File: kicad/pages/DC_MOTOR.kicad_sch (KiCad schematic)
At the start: 15 parts

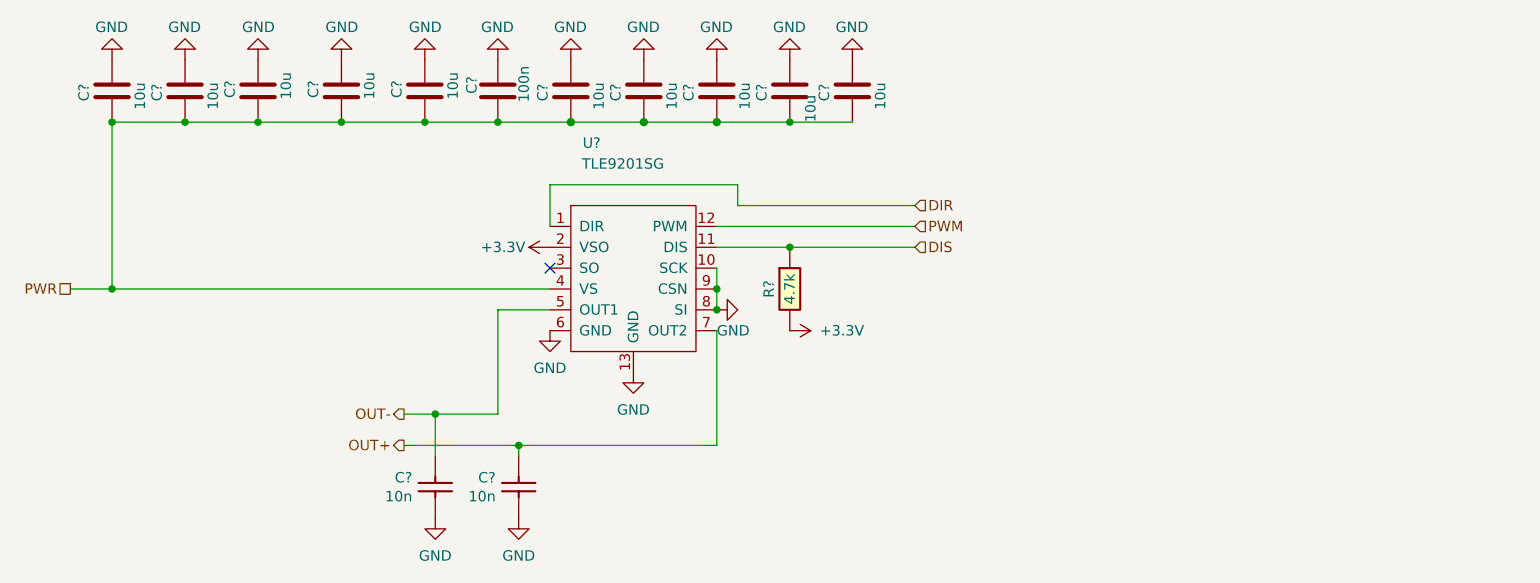
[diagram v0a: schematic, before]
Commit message: Update DC_MOTOR.kicad_sch
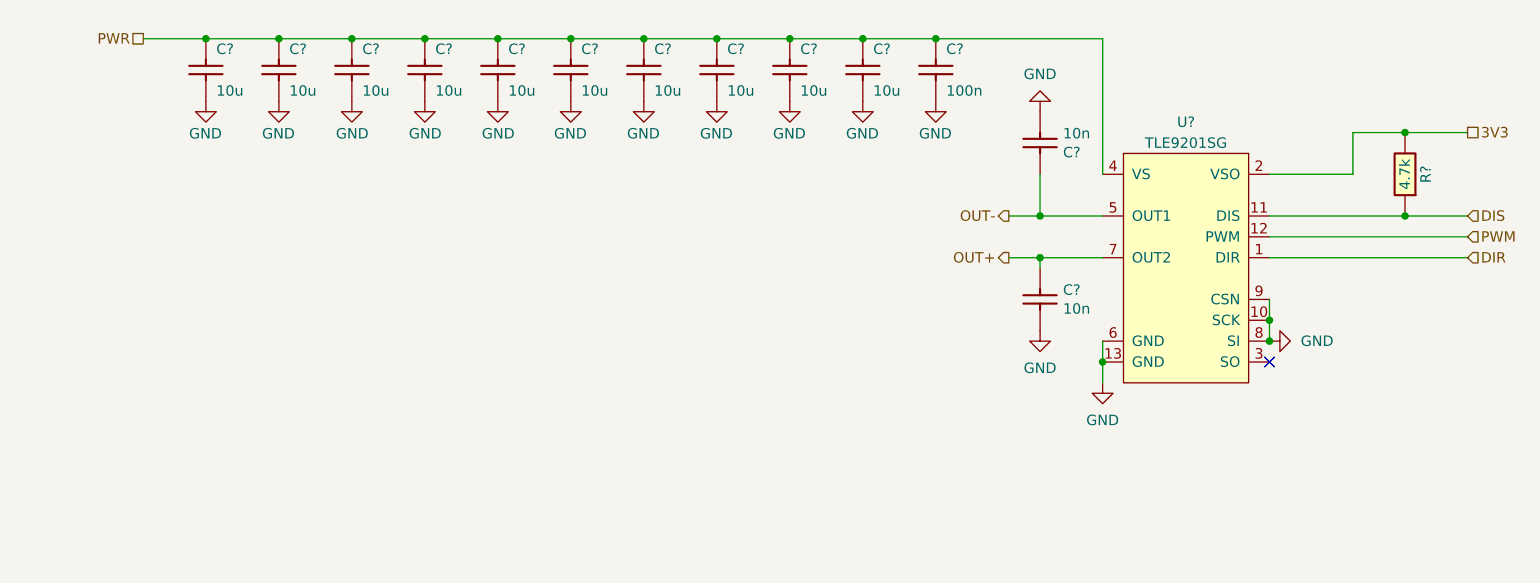
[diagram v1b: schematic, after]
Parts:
- removed C? (x10): 10u, hellen-one-common:C0805, symbol Device:C
- removed C?: 100n, hellen-one-common:C0603, symbol Device:C
- removed U?: TLE9201SG, Package_SO:Infineon_PG-DSO-12-11, symbol rusefi_tle9201:TLE9201SG
- added C? (x10): 10u, hellen-one-common:C0805, symbol hellen-one-common:Cap
- added C?: 100n, hellen-one-common:C0603, symbol hellen-one-common:Cap
- added U?: TLE9201SG, Package_SO:Infineon_PG-DSO-12-11, symbol chips:TLE9201SG
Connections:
- net DIR: now also U?.1 (DIR)
- net DIS: now also U?.11 (DIS)
- net GND: now also C?.1, C?.1, C?.1, C?.1, C?.1, C?.1, C?.1, C?.1, C?.1, C?.1, C?.1, U?.10 (SCK), U?.13 (GND), U?.6 (GND), U?.8 (SI), U?.9 (CSN)
- net OUT+: now also U?.7 (OUT2)
- net OUT-: now also U?.5 (OUT1)
- net PWM: now also U?.12 (PWM)
- net PWR: now also C?.2, C?.2, C?.2, C?.2, C?.2, C?.2, C?.2, C?.2, C?.2, C?.2, C?.2, U?.4 (VS)
- net +3.3V renamed 3V3
- net 3V3: now also U?.2 (VSO)
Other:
- title: (none) -> Hellen-One DC motor driver
- moved on the sheet: C?, R?
